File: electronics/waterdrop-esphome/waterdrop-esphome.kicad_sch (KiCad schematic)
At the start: 3 parts, among them J1 Barrel_Jack, U2 ESP32-S3-Tiny

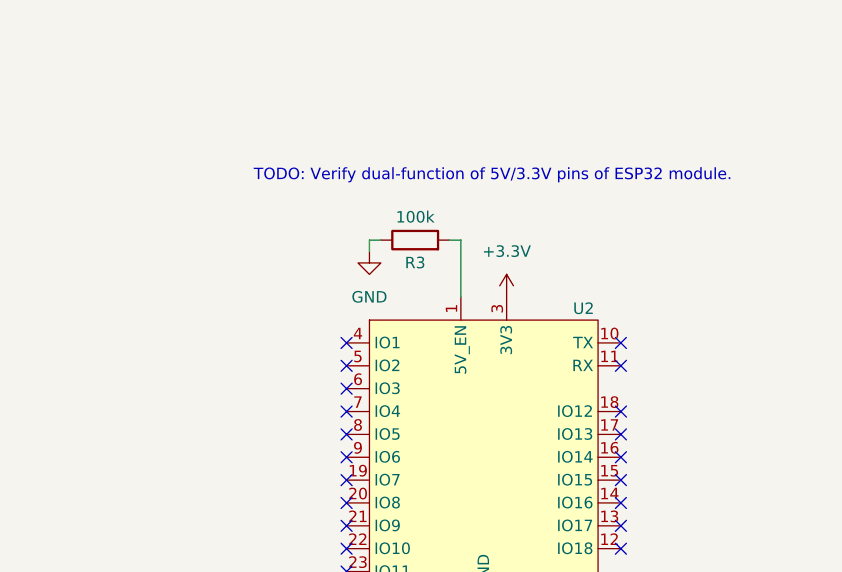
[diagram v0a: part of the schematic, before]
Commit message: ESP32-S3-Tiny doesn't have dual-purpose power pins, it requires 5V supply
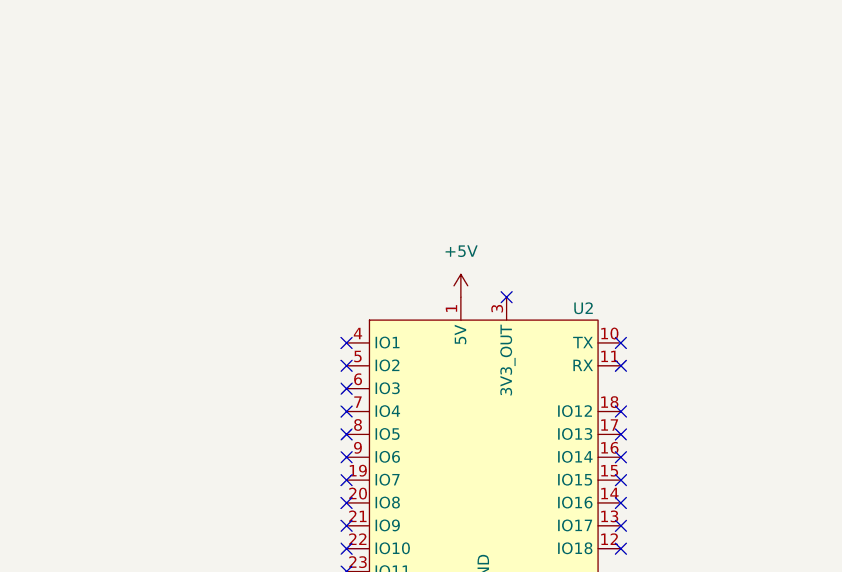
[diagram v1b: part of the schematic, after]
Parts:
- removed R3: 100k, Resistor_SMD:R_0805_2012Metric_Pad1.20x1.40mm_HandSolder, symbol Device:R
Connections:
- net +5V: now reaches U2.1 (5V)
- net +3.3V: no longer names the net of U2.3 (3V3_OUT)
- no-connect marks 20 -> 21
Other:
- note removed: "TODO: Verify dual-function of 5V/3.3V pins of ESP32 module."
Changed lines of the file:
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@@
 		(company "Tomasz Wasilczyk")
-	)
-	(text "TODO: Verify dual-function of 5V/3.3V pins of ESP32 module."
-		(exclude_from_sim no)
-		(at 140.716 76.708 0)
-		(effects
-			(font
-				(size 1.27 1.27)
-			)
-		)
 	)
 	(junction
@@
 	)
 	(no_connect
+		(at 142.24 90.17)
+	)
+	(no_connect
 		(at 154.94 110.49)
 	)
@@
 	(wire
 		(pts
-			(xy 137.16 83.82) (xy 137.16 90.17)
+			(xy 38.1 35.56) (xy 40.64 35.56)
 		)
 		(stroke
@@
 	(wire
 		(pts
-			(xy 38.1 35.56) (xy 40.64 35.56)
+			(xy 40.64 35.56) (xy 40.64 38.1)
 		)
 		(stroke
@@
 	(wire
 		(pts
-			(xy 40.64 35.56) (xy 40.64 38.1)
-		)
-		(stroke
-			(width 0)
-			(type default)
-		)
-	)
-	(wire
-		(pts
 			(xy 38.1 30.48) (xy 57.15 30.48)
-		)
-		(stroke
-			(width 0)
-			(type default)
-		)
-	)
-	(wire
-		(pts
-			(xy 135.89 83.82) (xy 137.16 83.82)
-		)
-		(stroke
-			(width 0)
-			(type default)
-		)
-	)
-	(wire
-		(pts
-			(xy 127 85.09) (xy 127 83.82)
-		)
-		(stroke
-			(width 0)
-			(type default)
-		)
-	)
-	(wire
-		(pts
-			(xy 127 83.82) (xy 128.27 83.82)
 		)
 		(stroke
@@
 	)
 	(symbol
-		(lib_id "power:+3.3V")
-		(at 142.24 90.17 0)
-		(unit 1)
-		(exclude_from_sim no)
-		(in_bom yes)
-		(on_board yes)
-		(dnp no)
-		(fields_autoplaced yes)
-		(property "Reference" "#PWR07"
-			(at 142.24 93.98 0)
-			(effects
-				(font
-					(size 1.27 1.27)
-				)
-				(hide yes)
-			)
-		)
-		(property "Value" "+3.3V"
-			(at 142.24 85.09 0)
-			(effects
-				(font
-					(size 1.27 1.27)
-				)
-			)
-		)
-		(property "Footprint" ""
-			(at 142.24 90.17 0)
-			(effects
-				(font
-					(size 1.27 1.27)
-				)
-				(hide yes)
-			)
-		)
-		(property "Datasheet" ""
-			(at 142.24 90.17 0)
-			(effects
-				(font
-					(size 1.27 1.27)
-				)
-				(hide yes)
-			)
-		)
-		(property "Description" "Power symbol creates a global label with name \"+3.3V\""
-			(at 142.24 90.17 0)
-			(effects
-				(font
-					(size 1.27 1.27)
-				)
-				(hide yes)
-			)
-		)
-		(pin "1"
-		)
-		(instances
-			(project ""
-				(path "/35f74f22-9f08-4dab-aa3a-794dd2e7ee12"
-					(reference "#PWR07")
-					(unit 1)
-				)
-			)
-		)
-	)
-	(symbol
 		(lib_id "power:GND")
 		(at 40.64 38.1 0)
@@
 	)
 	(symbol
+		(lib_id "power:+5V")
+		(at 137.16 90.17 0)
+		(unit 1)
+		(exclude_from_sim no)
+		(in_bom yes)
+		(on_board yes)
+		(dnp no)
+		(fields_autoplaced yes)
+		(property "Reference" "#PWR07"
+			(at 137.16 93.98 0)
+			(effects
+				(font
+					(size 1.27 1.27)
+				)
+				(hide yes)
+			)
+		)
+		(property "Value" "+5V"
+			(at 137.16 85.09 0)
+			(effects
+				(font
+					(size 1.27 1.27)
+				)
+			)
+		)
+		(property "Footprint" ""
+			(at 137.16 90.17 0)
+			(effects
+				(font
+					(size 1.27 1.27)
+				)
+				(hide yes)
+			)
+		)
+		(property "Datasheet" ""
+			(at 137.16 90.17 0)
+			(effects
+				(font
+					(size 1.27 1.27)
+				)
+				(hide yes)
+			)
+		)
+		(property "Description" "Power symbol creates a global label with name \"+5V\""
+			(at 137.16 90.17 0)
+			(effects
+				(font
+					(size 1.27 1.27)
+				)
+				(hide yes)
+			)
+		)
+		(pin "1"
+		)
+		(instances
+			(project ""
+				(path "/35f74f22-9f08-4dab-aa3a-794dd2e7ee12"
+					(reference "#PWR07")
+					(unit 1)
+				)
+			)
+		)
+	)
+	(symbol
 		(lib_id "RF_Module_extra:ESP32-S3-TINY")
 		(at 139.7 107.95 0)
@@
 		)
 		(pin "3"
-			(alternate "3V3")
 		)
 		(pin "10"
@@
 		)
 		(pin "1"
-			(alternate "5V_EN")
 		)
 		(pin "7"
@@
 				(path "/35f74f22-9f08-4dab-aa3a-794dd2e7ee12"
 					(reference "U2")
-					(unit 1)
-				)
-			)
-		)
-	)
-	(symbol
-		(lib_id "power:GND")
-		(at 127 85.09 0)
-		(unit 1)
-		(exclude_from_sim no)
-		(in_bom yes)
-		(on_board yes)
-		(dnp no)
-		(fields_autoplaced yes)
-		(property "Reference" "#PWR08"
-			(at 127 91.44 0)
-			(effects
-				(font
-					(size 1.27 1.27)
-				)
-				(hide yes)
-			)
-		)
-		(property "Value" "GND"
-			(at 127 90.17 0)
-			(effects
-				(font
-					(size 1.27 1.27)
-				)
-			)
-		)
-		(property "Footprint" ""
-			(at 127 85.09 0)
-			(effects
-				(font
-					(size 1.27 1.27)
-				)
-				(hide yes)
-			)
-		)
-		(property "Datasheet" ""
-			(at 127 85.09 0)
-			(effects
-				(font
-					(size 1.27 1.27)
-				)
-				(hide yes)
-			)
-		)
-		(property "Description" "Power symbol creates a global label with name \"GND\" , ground"
-			(at 127 85.09 0)
-			(effects
-				(font
-					(size 1.27 1.27)
-				)
-				(hide yes)
-			)
-		)
-		(pin "1"
-		)
-		(instances
-			(project ""
-				(path "/35f74f22-9f08-4dab-aa3a-794dd2e7ee12"
-					(reference "#PWR08")
 					(unit 1)
 				)
@@
 					(unit 1)
 				)
-			)
-		)
-	)
-	(symbol
-		(lib_id "Device:R")
-		(at 132.08 83.82 90)
-		(unit 1)
-		(exclude_from_sim no)
-		(in_bom yes)
-		(on_board yes)
-		(dnp no)
-		(property "Reference" "R3"
-			(at 132.08 86.36 90)
-			(effects
-				(font
-					(size 1.27 1.27)
-				)
-			)
-		)
-		(property "Value" "100k"
-			(at 132.08 81.28 90)
-			(effects
-				(font
-					(size 1.27 1.27)
-				)
-			)
-		)
-		(property "Footprint" "Resistor_SMD:R_0805_2012Metric_Pad1.20x1.40mm_HandSolder"
-			(at 132.08 85.598 90)
-			(effects
-				(font
-					(size 1.27 1.27)
-				)
-				(hide yes)
-			)
-		)
-		(property "Datasheet" "~"
-			(at 132.08 83.82 0)
-			(effects
-				(font
-					(size 1.27 1.27)
-				)
-				(hide yes)
-			)
-		)
-		(property "Description" "Resistor"
-			(at 132.08 83.82 0)
-			(effects
-				(font
-					(size 1.27 1.27)
-				)
-				(hide yes)
-			)
-		)
-		(pin "2"
-		)
-		(pin "1"
-		)
-		(instances
-			(project ""
-				(path "/35f74f22-9f08-4dab-aa3a-794dd2e7ee12"
-					(reference "R3")
-					(unit 1)
-				)

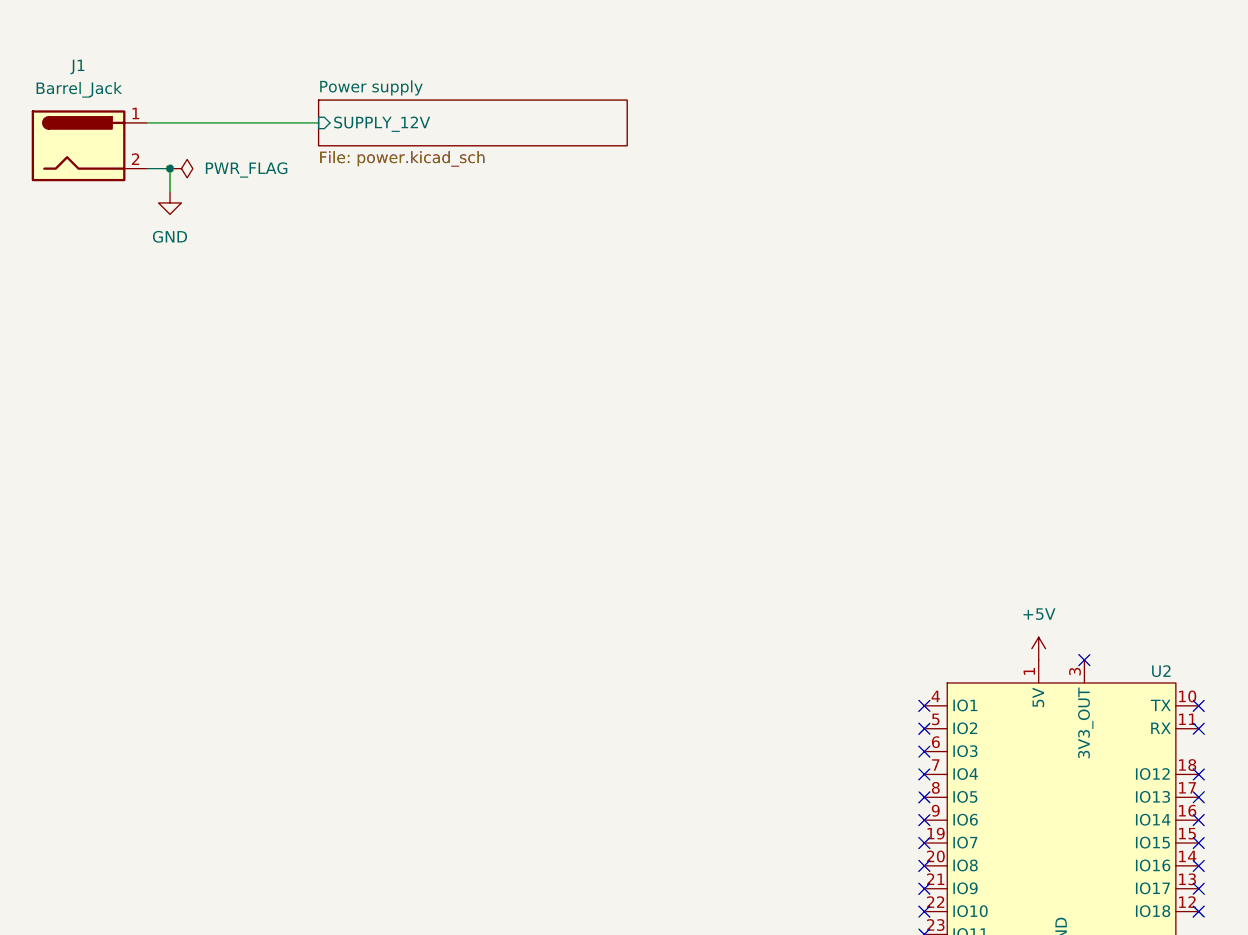
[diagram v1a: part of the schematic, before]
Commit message: Schematics for 12V circuit, describe serial level converter
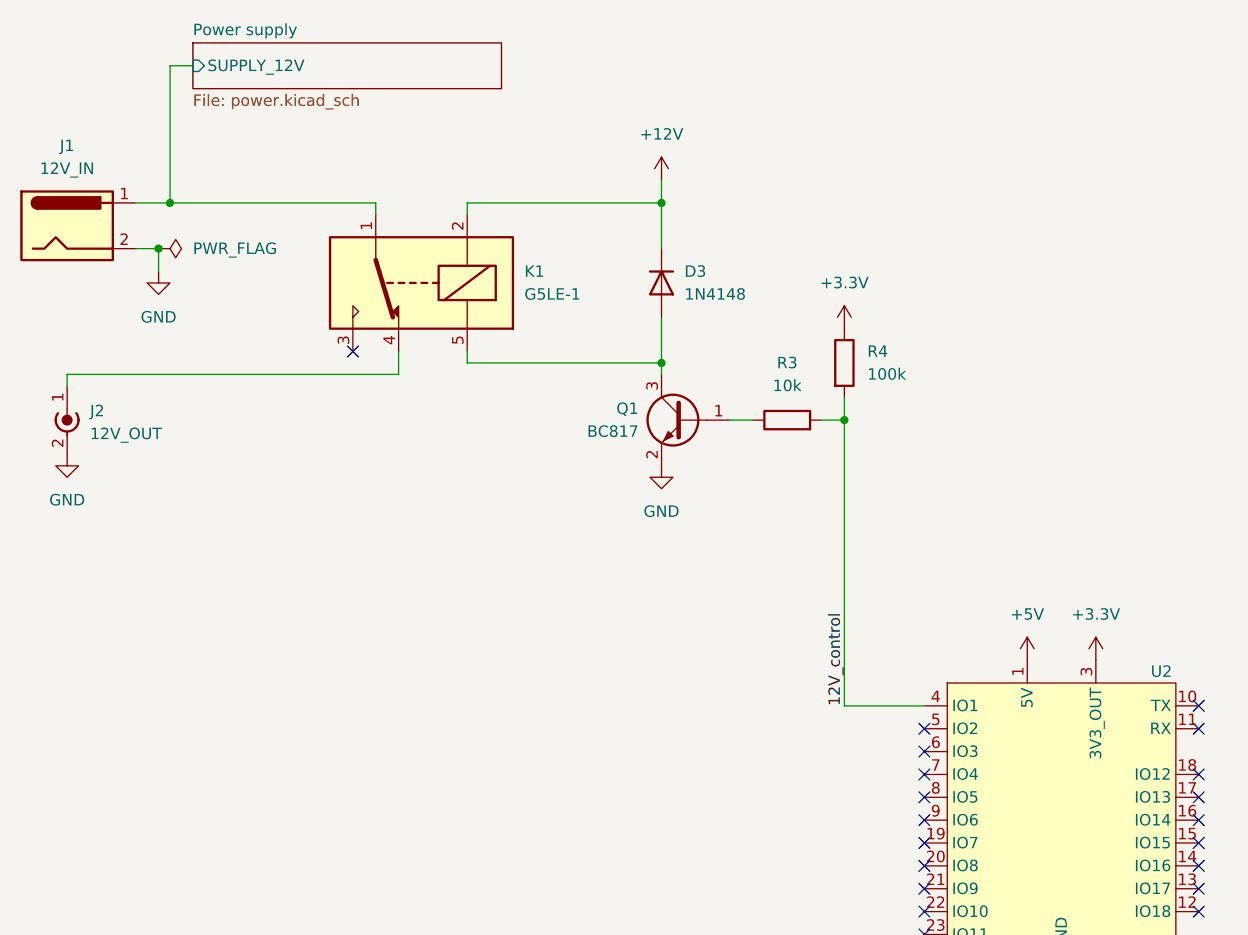
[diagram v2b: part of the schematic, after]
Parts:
- added D3: 1N4148, Diode_THT:D_DO-35_SOD27_P7.62mm_Horizontal, symbol Diode:1N4148
- added J2: 12V_OUT, Connector_Wire:SolderWire-1sqmm_1x02_P5.4mm_D1.4mm_OD2.7mm_Relief, symbol Connector:Conn_Coaxial_Power
- added K1: G5LE-1, Relay_THT:Relay_SPDT_Omron-G5LE-1, symbol Relay:G5LE-1
- added Q1: BC817, Package_TO_SOT_SMD:SOT-23, symbol Transistor_BJT:BC817
- added R3: 10k, symbol Device:R
- added R4: 100k, symbol Device:R
- J1: value Barrel_Jack -> 12V_IN
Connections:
- net GND: now also J2.2 (Ext), Q1.2 (E)
- net Power supply/SUPPLY_12V: now also K1.1
- net +3.3V: now reaches U2.3 (3V3_OUT)
- net +3.3V: now also R4.1
- net 12V_control: now reaches U2.4 (IO1)
- net 12V_control: now also R3.2, R4.2
- new net: Q1.1 (B), R3.1
- new net: D3.2 (A), K1.5, Q1.3 (C)
- new net: J2.1 (In), K1.4
- new net +12V: D3.1 (K), K1.2
- no-connect marks 21 -> 20
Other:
- moved on the sheet: J1

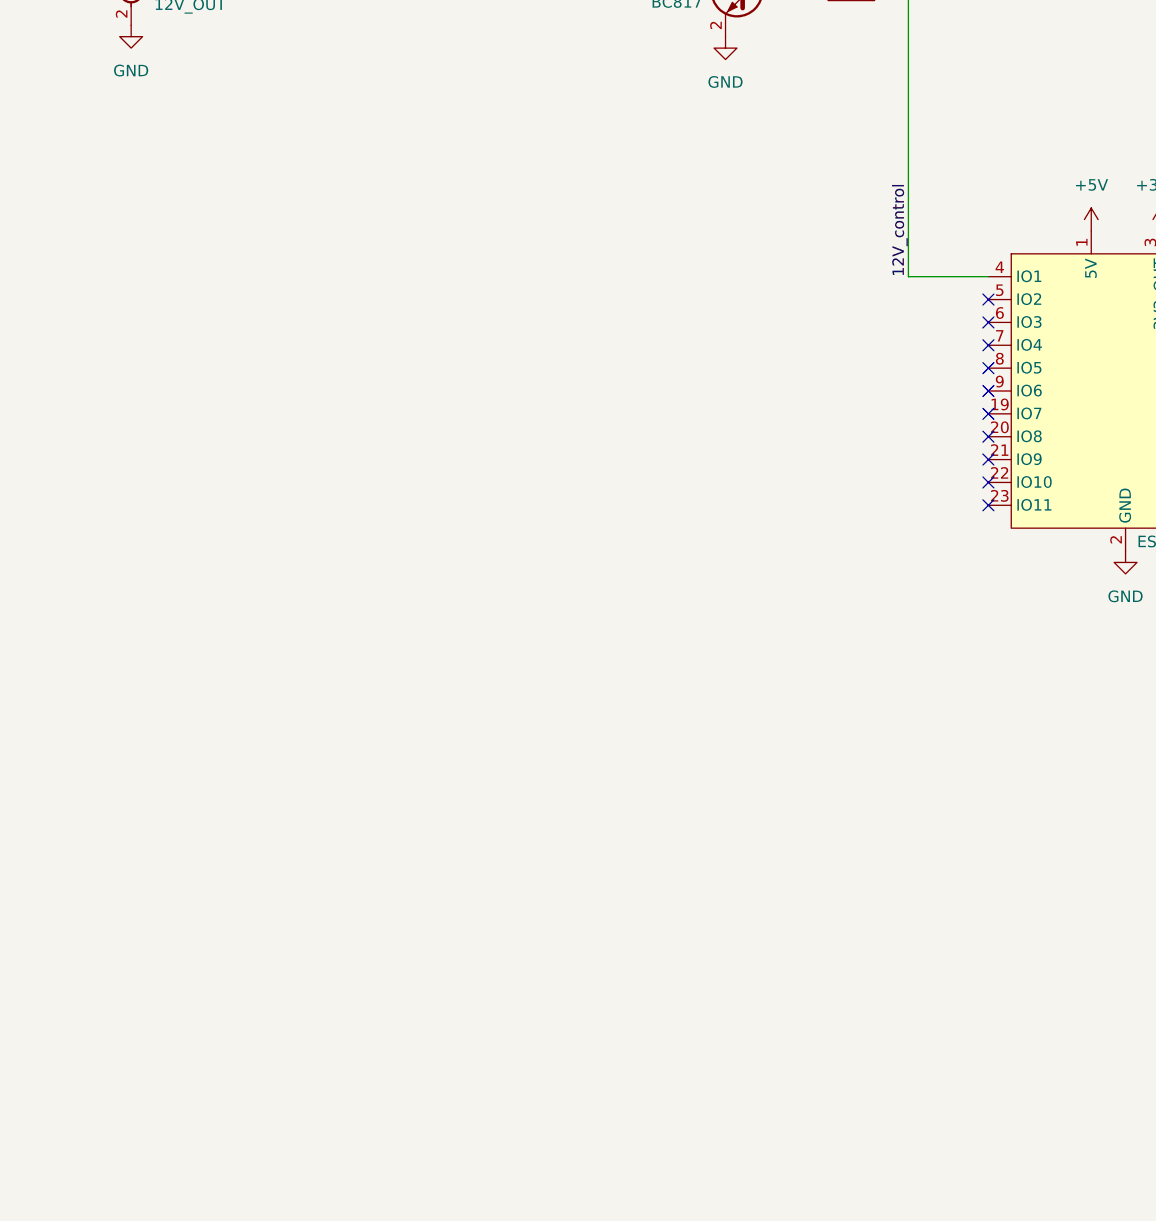
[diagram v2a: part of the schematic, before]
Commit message: Schematics for serial communication
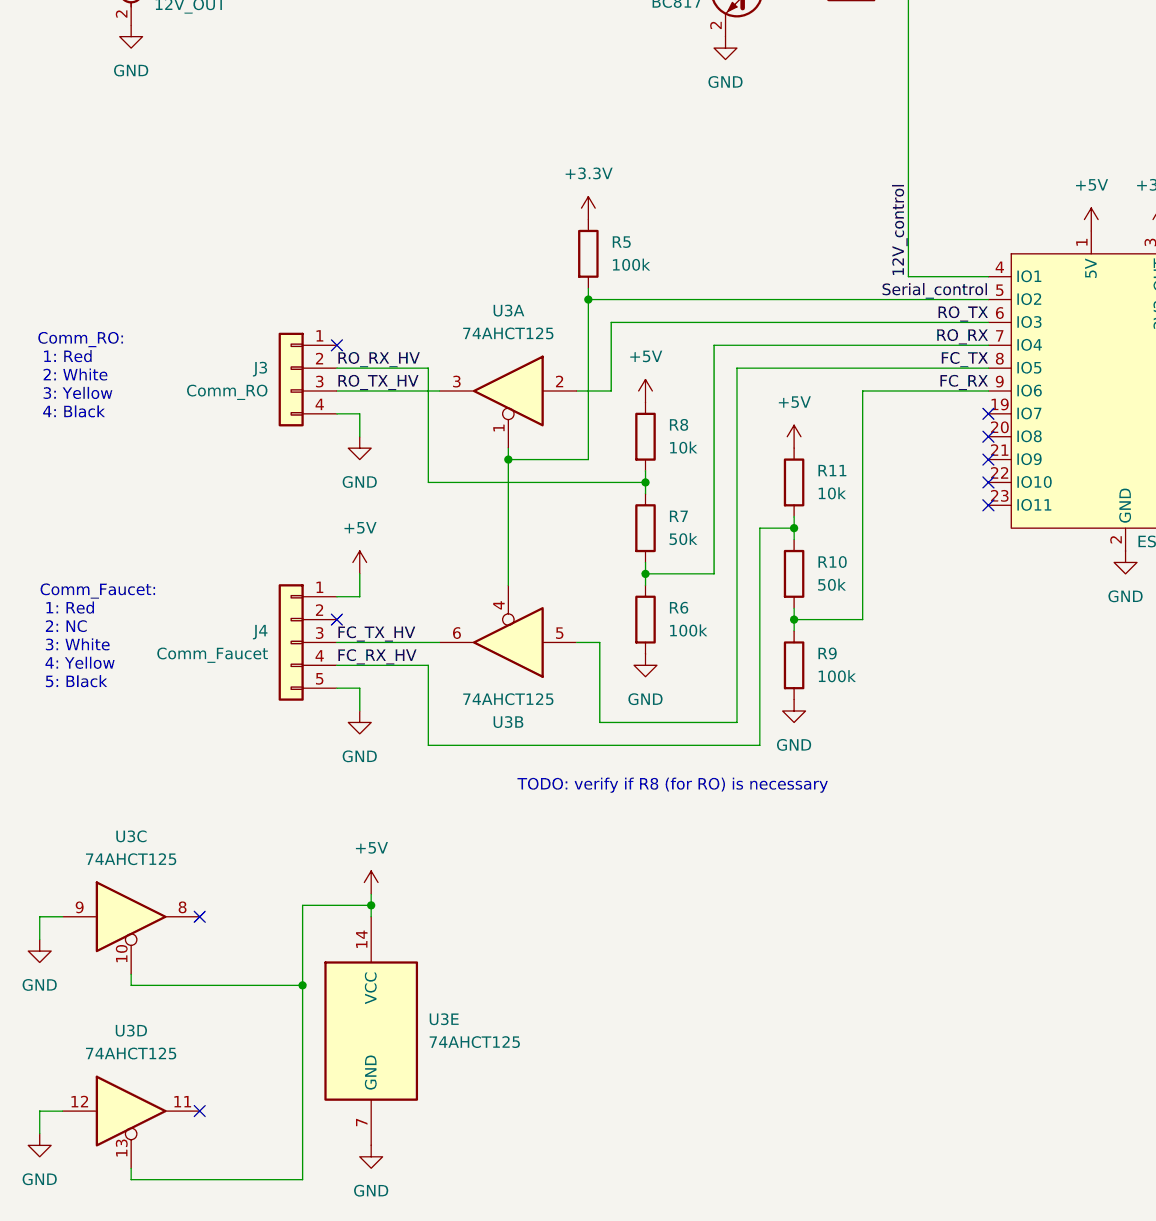
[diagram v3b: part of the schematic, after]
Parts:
- added J3: Comm_RO, symbol Connector_Generic:Conn_01x04
- added J4: Comm_Faucet, symbol Connector_Generic:Conn_01x05
- added R10, R7: 50k, symbol Device:R
- added R11, R8: 10k, symbol Device:R
- added R5, R6, R9: 100k, symbol Device:R
- added U3: 74AHCT125, symbol 74xx:74AHCT125
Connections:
- net +3.3V: now also R5.1
- net +5V: now also J4.1 (Pin_1), R11.1, R8.1, U3.10, U3.13, U3.14 (VCC)
- net GND: now also J3.4 (Pin_4), J4.5 (Pin_5), R6.2, R9.2, U3.12, U3.7 (GND), U3.9
- net Serial_control: now reaches U2.5 (IO2)
- net Serial_control: now also R5.2, U3.1, U3.4
- net RO_TX: now reaches U2.6 (IO3)
- net RO_TX: now also U3.2
- net RO_RX: now reaches U2.7 (IO4)
- net RO_RX: now also R6.1, R7.2
- net FC_TX: now reaches U2.8 (IO5)
- net FC_TX: now also U3.5
- net FC_RX: now reaches U2.9 (IO6)
- net FC_RX: now also R10.2, R9.1
- new net FC_RX_HV: J4.4 (Pin_4), R10.1, R11.2
- new net FC_TX_HV: J4.3 (Pin_3), U3.6
- new net RO_RX_HV: J3.2 (Pin_2), R7.1, R8.2
- new net RO_TX_HV: J3.3 (Pin_3), U3.3
- no-connect marks 20 -> 19
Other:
- note added: "Comm_Faucet: 1: Red 2: NC 3: White 4: Yellow 5: Black"
- note added: "Comm_RO: 1: Red 2: White 3: Yellow 4: Black"
- note added: "TODO: verify if R8 (for RO) is necessary"
